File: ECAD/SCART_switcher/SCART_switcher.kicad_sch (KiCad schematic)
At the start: 8 parts

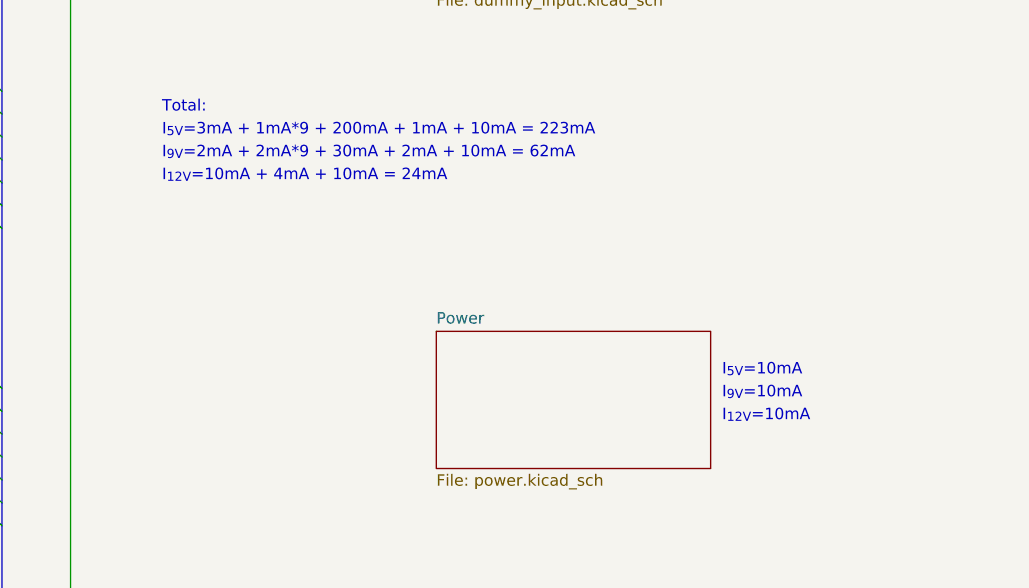
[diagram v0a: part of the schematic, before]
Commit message: Update SCART_switcher.kicad_sch
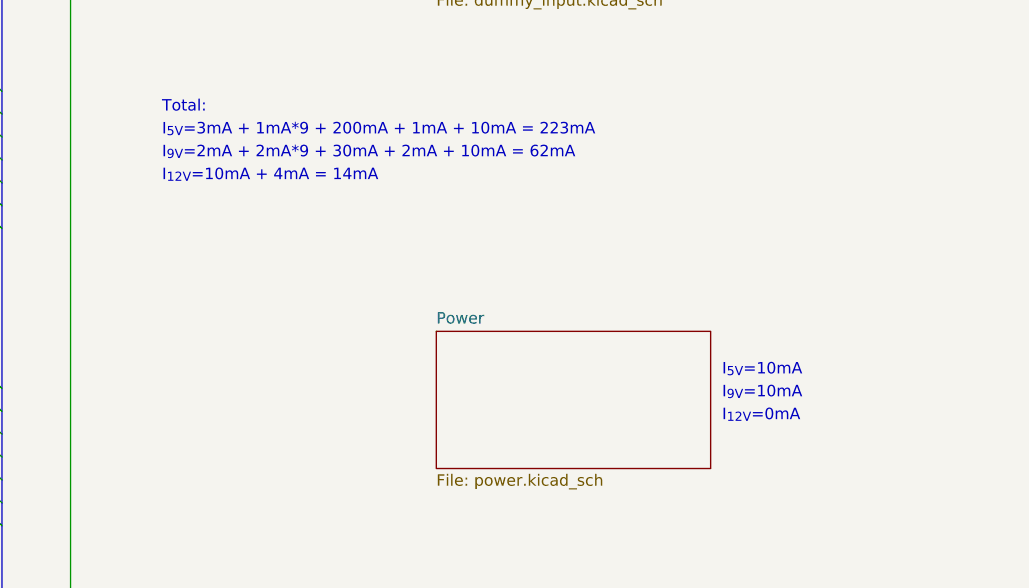
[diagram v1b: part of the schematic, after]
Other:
- note added: "I_{12V}=10mA + 4mA = 14mA"
- note removed: "I_{12V}=10mA"
- note removed: "I_{12V}=10mA + 4mA + 10mA = 24mA"
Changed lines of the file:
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@@
     (effects (font (size 1.27 1.27)) (justify left bottom))
   )
-  (text "I_{12V}=10mA + 4mA + 10mA = 24mA" (at 175.26 104.14 0)
+  (text "I_{12V}=10mA + 4mA = 14mA" (at 175.26 104.14 0)
     (effects (font (size 1.27 1.27)) (justify left bottom))
   )
@@
     (effects (font (size 1.27 1.27)) (justify left bottom))
   )
-  (text "I_{12V}=10mA" (at 237.49 130.81 0)
+  (text "I_{12V}=0mA" (at 237.49 130.81 0)
     (effects (font (size 1.27 1.27)) (justify left bottom))
   )

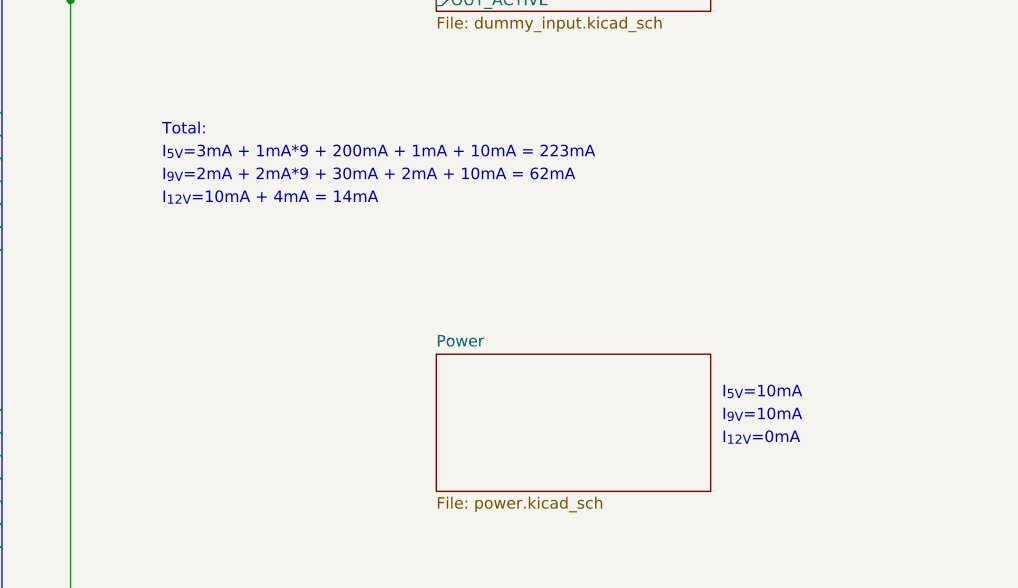
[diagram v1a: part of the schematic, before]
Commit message: Update SCART_switcher.kicad_sch
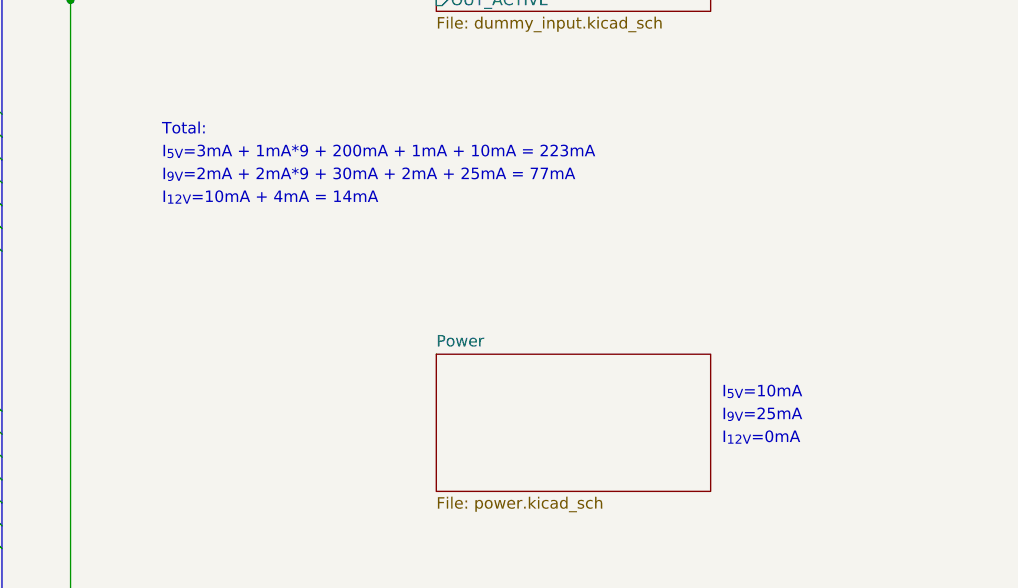
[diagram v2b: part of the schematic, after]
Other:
- note added: "I_{9V}=25mA"
- note added: "I_{9V}=2mA + 2mA*9 + 30mA + 2mA + 25mA = 77mA"
- note removed: "I_{9V}=10mA"
- note removed: "I_{9V}=2mA + 2mA*9 + 30mA + 2mA + 10mA = 62mA"
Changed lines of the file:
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@@
     (effects (font (size 1.27 1.27)) (justify left bottom))
   )
-  (text "I_{9V}=2mA + 2mA*9 + 30mA + 2mA + 10mA = 62mA" (at 175.26 101.6 0)
+  (text "I_{9V}=2mA + 2mA*9 + 30mA + 2mA + 25mA = 77mA" (at 175.26 101.6 0)
     (effects (font (size 1.27 1.27)) (justify left bottom))
   )
@@
     (effects (font (size 1.27 1.27)) (justify left bottom))
   )
-  (text "I_{9V}=10mA" (at 237.49 128.27 0)
+  (text "I_{9V}=25mA" (at 237.49 128.27 0)
     (effects (font (size 1.27 1.27)) (justify left bottom))
   )

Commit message: Progressed ECAD.
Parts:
- H1, H2, H3, H4, H5, H6, H7, H8: MPN_MOUSER (none) -> N/A
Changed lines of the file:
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@@
       (effects (font (size 1.27 1.27)) hide)
     )
-    (property "Datasheet" "~" (at 190.5 160.02 0)
+    (property "Datasheet" "N/A" (at 190.5 160.02 0)
       (effects (font (size 1.27 1.27)) hide)
     )
@@
       (effects (font (size 1.27 1.27)) hide)
     )
-    (property "MPN_MOUSER" "" (at 190.5 160.02 0)
+    (property "MPN_MOUSER" "N/A" (at 190.5 160.02 0)
       (effects (font (size 1.27 1.27)) hide)
     )
@@
       (effects (font (size 1.27 1.27)) hide)
     )
-    (property "Datasheet" "~" (at 190.5 153.67 0)
+    (property "Datasheet" "N/A" (at 190.5 153.67 0)
       (effects (font (size 1.27 1.27)) hide)
     )
@@
       (effects (font (size 1.27 1.27)) hide)
     )
-    (property "MPN_MOUSER" "" (at 190.5 153.67 0)
+    (property "MPN_MOUSER" "N/A" (at 190.5 153.67 0)
       (effects (font (size 1.27 1.27)) hide)
     )
@@
       (effects (font (size 1.27 1.27)) hide)
     )
-    (property "Datasheet" "~" (at 231.14 153.67 0)
+    (property "Datasheet" "N/A" (at 231.14 153.67 0)
       (effects (font (size 1.27 1.27)) hide)
     )
@@
       (effects (font (size 1.27 1.27)) hide)
     )
-    (property "MPN_MOUSER" "" (at 231.14 153.67 0)
+    (property "MPN_MOUSER" "N/A" (at 231.14 153.67 0)
       (effects (font (size 1.27 1.27)) hide)
     )
@@
       (effects (font (size 1.27 1.27)) hide)
     )
-    (property "Datasheet" "~" (at 231.14 160.02 0)
+    (property "Datasheet" "N/A" (at 231.14 160.02 0)
       (effects (font (size 1.27 1.27)) hide)
     )
@@
       (effects (font (size 1.27 1.27)) hide)
     )
-    (property "MPN_MOUSER" "" (at 231.14 160.02 0)
+    (property "MPN_MOUSER" "N/A" (at 231.14 160.02 0)
       (effects (font (size 1.27 1.27)) hide)
     )
@@
       (effects (font (size 1.27 1.27)) hide)
     )
-    (property "Datasheet" "~" (at 210.82 160.02 0)
+    (property "Datasheet" "N/A" (at 210.82 160.02 0)
       (effects (font (size 1.27 1.27)) hide)
     )
@@
       (effects (font (size 1.27 1.27)) hide)
     )
-    (property "MPN_MOUSER" "" (at 210.82 160.02 0)
+    (property "MPN_MOUSER" "N/A" (at 210.82 160.02 0)
       (effects (font (size 1.27 1.27)) hide)
     )
@@
       (effects (font (size 1.27 1.27)) hide)
     )
-    (property "Datasheet" "~" (at 251.46 153.67 0)
+    (property "Datasheet" "N/A" (at 251.46 153.67 0)
       (effects (font (size 1.27 1.27)) hide)
     )
@@
       (effects (font (size 1.27 1.27)) hide)
     )
-    (property "MPN_MOUSER" "" (at 251.46 153.67 0)
+    (property "MPN_MOUSER" "N/A" (at 251.46 153.67 0)
       (effects (font (size 1.27 1.27)) hide)
     )
@@
       (effects (font (size 1.27 1.27)) hide)
     )
-    (property "Datasheet" "~" (at 251.46 160.02 0)
+    (property "Datasheet" "N/A" (at 251.46 160.02 0)
       (effects (font (size 1.27 1.27)) hide)
     )
@@
       (effects (font (size 1.27 1.27)) hide)
     )
-    (property "MPN_MOUSER" "" (at 251.46 160.02 0)
+    (property "MPN_MOUSER" "N/A" (at 251.46 160.02 0)
       (effects (font (size 1.27 1.27)) hide)
     )
@@
       (effects (font (size 1.27 1.27)) hide)
     )
-    (property "Datasheet" "~" (at 210.82 153.67 0)
+    (property "Datasheet" "N/A" (at 210.82 153.67 0)
       (effects (font (size 1.27 1.27)) hide)
     )
@@
       (effects (font (size 1.27 1.27)) hide)
     )
-    (property "MPN_MOUSER" "" (at 210.82 153.67 0)
-      (effects (font (size 1.27 1.27)) hide)
-    )
+    (property "MPN_MOUSER" "N/A" (at 210.82 153.67 0)
+      (effects (font (size 1.27 1.27)) hide)
+    )

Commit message: Progressed ECAD
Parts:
- H1, H2, H3, H4, H5, H6, H7, H8: MPN N/A -> (none); MPN_MOUSER N/A -> (none)
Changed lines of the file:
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@@
       (effects (font (size 1.27 1.27)) hide)
     )
-    (property "MPN" "N/A" (at 190.5 160.02 0)
-      (effects (font (size 1.27 1.27)) hide)
-    )
-    (property "MPN_MOUSER" "N/A" (at 190.5 160.02 0)
+    (property "MPN" "" (at 190.5 160.02 0)
+      (effects (font (size 1.27 1.27)) hide)
+    )
+    (property "MPN_MOUSER" "" (at 190.5 160.02 0)
       (effects (font (size 1.27 1.27)) hide)
     )
@@
       (effects (font (size 1.27 1.27)) hide)
     )
-    (property "MPN" "N/A" (at 190.5 153.67 0)
-      (effects (font (size 1.27 1.27)) hide)
-    )
-    (property "MPN_MOUSER" "N/A" (at 190.5 153.67 0)
+    (property "MPN" "" (at 190.5 153.67 0)
+      (effects (font (size 1.27 1.27)) hide)
+    )
+    (property "MPN_MOUSER" "" (at 190.5 153.67 0)
       (effects (font (size 1.27 1.27)) hide)
     )
@@
       (effects (font (size 1.27 1.27)) hide)
     )
-    (property "MPN" "N/A" (at 231.14 153.67 0)
-      (effects (font (size 1.27 1.27)) hide)
-    )
-    (property "MPN_MOUSER" "N/A" (at 231.14 153.67 0)
+    (property "MPN" "" (at 231.14 153.67 0)
+      (effects (font (size 1.27 1.27)) hide)
+    )
+    (property "MPN_MOUSER" "" (at 231.14 153.67 0)
       (effects (font (size 1.27 1.27)) hide)
     )
@@
       (effects (font (size 1.27 1.27)) hide)
     )
-    (property "MPN" "N/A" (at 231.14 160.02 0)
-      (effects (font (size 1.27 1.27)) hide)
-    )
-    (property "MPN_MOUSER" "N/A" (at 231.14 160.02 0)
+    (property "MPN" "" (at 231.14 160.02 0)
+      (effects (font (size 1.27 1.27)) hide)
+    )
+    (property "MPN_MOUSER" "" (at 231.14 160.02 0)
       (effects (font (size 1.27 1.27)) hide)
     )
@@
       (effects (font (size 1.27 1.27)) hide)
     )
-    (property "MPN" "N/A" (at 210.82 160.02 0)
-      (effects (font (size 1.27 1.27)) hide)
-    )
-    (property "MPN_MOUSER" "N/A" (at 210.82 160.02 0)
+    (property "MPN" "" (at 210.82 160.02 0)
+      (effects (font (size 1.27 1.27)) hide)
+    )
+    (property "MPN_MOUSER" "" (at 210.82 160.02 0)
       (effects (font (size 1.27 1.27)) hide)
     )
@@
       (effects (font (size 1.27 1.27)) hide)
     )
-    (property "MPN" "N/A" (at 251.46 153.67 0)
-      (effects (font (size 1.27 1.27)) hide)
-    )
-    (property "MPN_MOUSER" "N/A" (at 251.46 153.67 0)
+    (property "MPN" "" (at 251.46 153.67 0)
+      (effects (font (size 1.27 1.27)) hide)
+    )
+    (property "MPN_MOUSER" "" (at 251.46 153.67 0)
       (effects (font (size 1.27 1.27)) hide)
     )
@@
       (effects (font (size 1.27 1.27)) hide)
     )
-    (property "MPN" "N/A" (at 251.46 160.02 0)
-      (effects (font (size 1.27 1.27)) hide)
-    )
-    (property "MPN_MOUSER" "N/A" (at 251.46 160.02 0)
+    (property "MPN" "" (at 251.46 160.02 0)
+      (effects (font (size 1.27 1.27)) hide)
+    )
+    (property "MPN_MOUSER" "" (at 251.46 160.02 0)
       (effects (font (size 1.27 1.27)) hide)
     )
@@
       (effects (font (size 1.27 1.27)) hide)
     )
-    (property "MPN" "N/A" (at 210.82 153.67 0)
-      (effects (font (size 1.27 1.27)) hide)
-    )
-    (property "MPN_MOUSER" "N/A" (at 210.82 153.67 0)
-      (effects (font (size 1.27 1.27)) hide)
-    )
+    (property "MPN" "" (at 210.82 153.67 0)
+      (effects (font (size 1.27 1.27)) hide)
+    )
+    (property "MPN_MOUSER" "" (at 210.82 153.67 0)
+      (effects (font (size 1.27 1.27)) hide)
+    )

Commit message: PRogressed ECAD.
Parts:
- removed H1, H2, H3, H4, H5, H6, H7, H8: MountingHole, MountingHole:MountingHole_3.2mm_M3, symbol Mechanical:MountingHole
